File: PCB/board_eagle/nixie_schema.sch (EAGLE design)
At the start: 55 parts, among them IC1 LM2672M

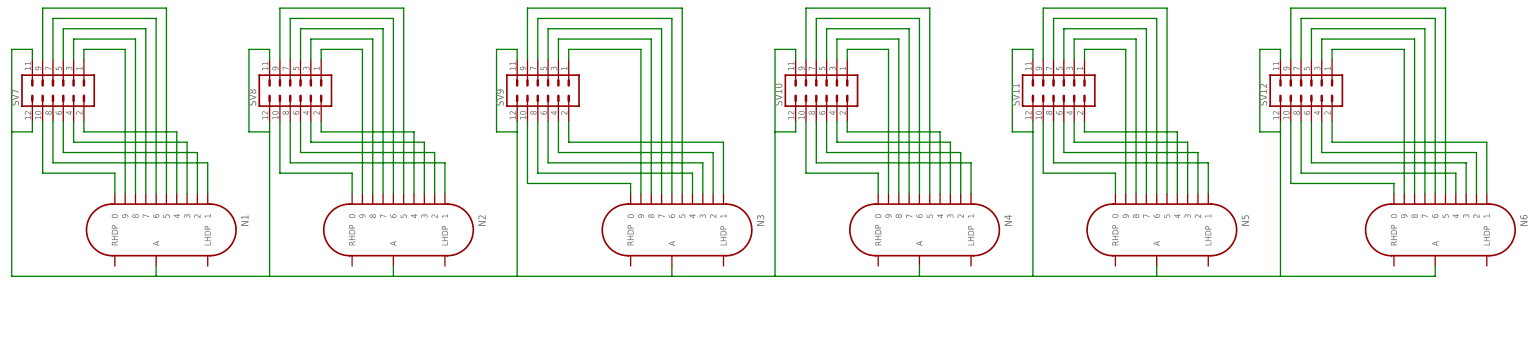
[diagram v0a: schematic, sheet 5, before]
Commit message: Fixing minor schematic issues (anode resistors and cap values in 3v3 PSU). Updated gitignore with EAGLE temp files
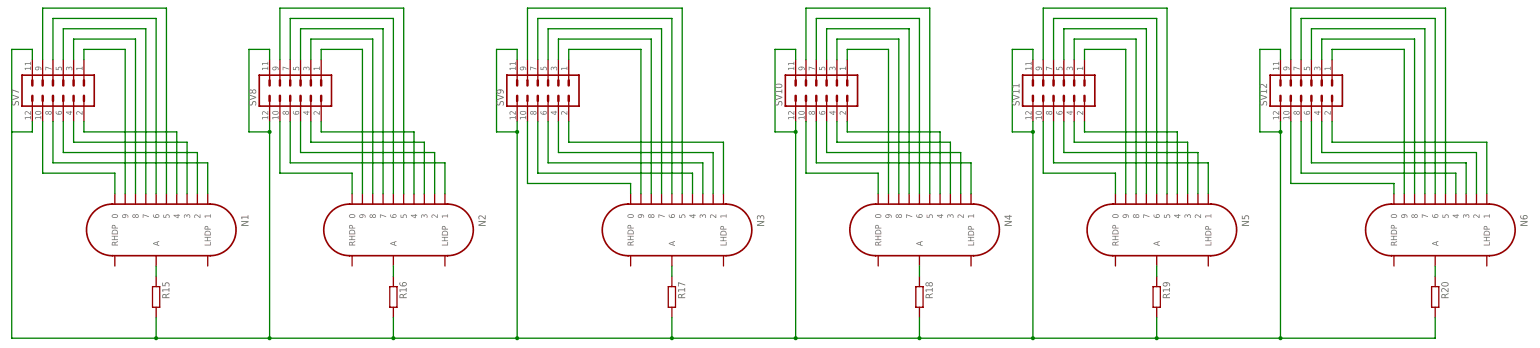
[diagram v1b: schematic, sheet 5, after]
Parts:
- added R15, R16, R17, R18, R19, R20: (no value), resistor:R-EU_R0603
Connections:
- removed net N$74: N1.A, N2.A, N3.A, N4.A, N5.A, N6.A, SV10.11, SV10.12, SV11.11, SV11.12, SV12.11, SV12.12, SV7.11, SV7.12, SV8.11, SV8.12, SV9.11, SV9.12
- new net N$45: R15.2, R16.2, R17.2, R18.2, R19.2, R20.2, SV10.11, SV10.12, SV11.11, SV11.12, SV12.11, SV12.12, SV7.11, SV7.12, SV8.11, SV8.12, SV9.11, SV9.12
- new net N$89: N6.A, R20.1
- new net N$90: N5.A, R19.1
- new net N$91: N4.A, R18.1
- new net N$92: N3.A, R17.1
- new net N$93: N2.A, R16.1
- new net N$94: N1.A, R15.1
- net GND: now also C6.C1; no longer C5.C1
- net N$11: now also C5.C1; no longer C6.C1
- net N$12: now also C5.C2; no longer C6.C2
- net N$5: now also C6.C2; no longer C5.C2
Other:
- moved on the sheet: C5, C6

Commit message: Most of HV supply schematic done. Need to pick transistors, caps and diode
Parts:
- added C10, C11: 680p, eagle-ltspice:C
- added D1: (no value), diode:DIODE-SOD123
- added Q1: (no value), semicon-smd-ipc:PNP-TRANSISTOR_SOT23
- added Q2: IRF3704S, transistor-power:IRF3704S
- added R21: 1k, resistor:R-EU_R0603
- added R22, R23: (no value), eagle-ltspice:RR1210
- added R24: 330k, resistor:R-EU_R0603
- added R25: 3.3k, resistor:R-EU_R0603
- added R26: 5.6k, resistor:R-EU_R0603
- added U$18: MC34063, MC34063:MC34063
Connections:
- new net N$74: C10.1, U$18.CT
- new net N$85: D1.A, Q1.B, R21.1, U$18.ES
- new net N$86: Q2.D
- new net N$87: R22.2, R23.2, U$18.CD, U$18.CS, U$18.IS
- new net N$95: D1.C, Q1.E, Q2.G
- new net N$96: C11.1, R24.2, R25.1, R26.1, U$18.CMP
- new net N$97: R26.2
- net GND: now also C10.2, C11.2, Q1.C, Q2.S, R21.2, R25.2, U$18.GND
- net HV_IN+: now also R24.1
- net VCC: now also R22.1, R23.1, U$18.VCC

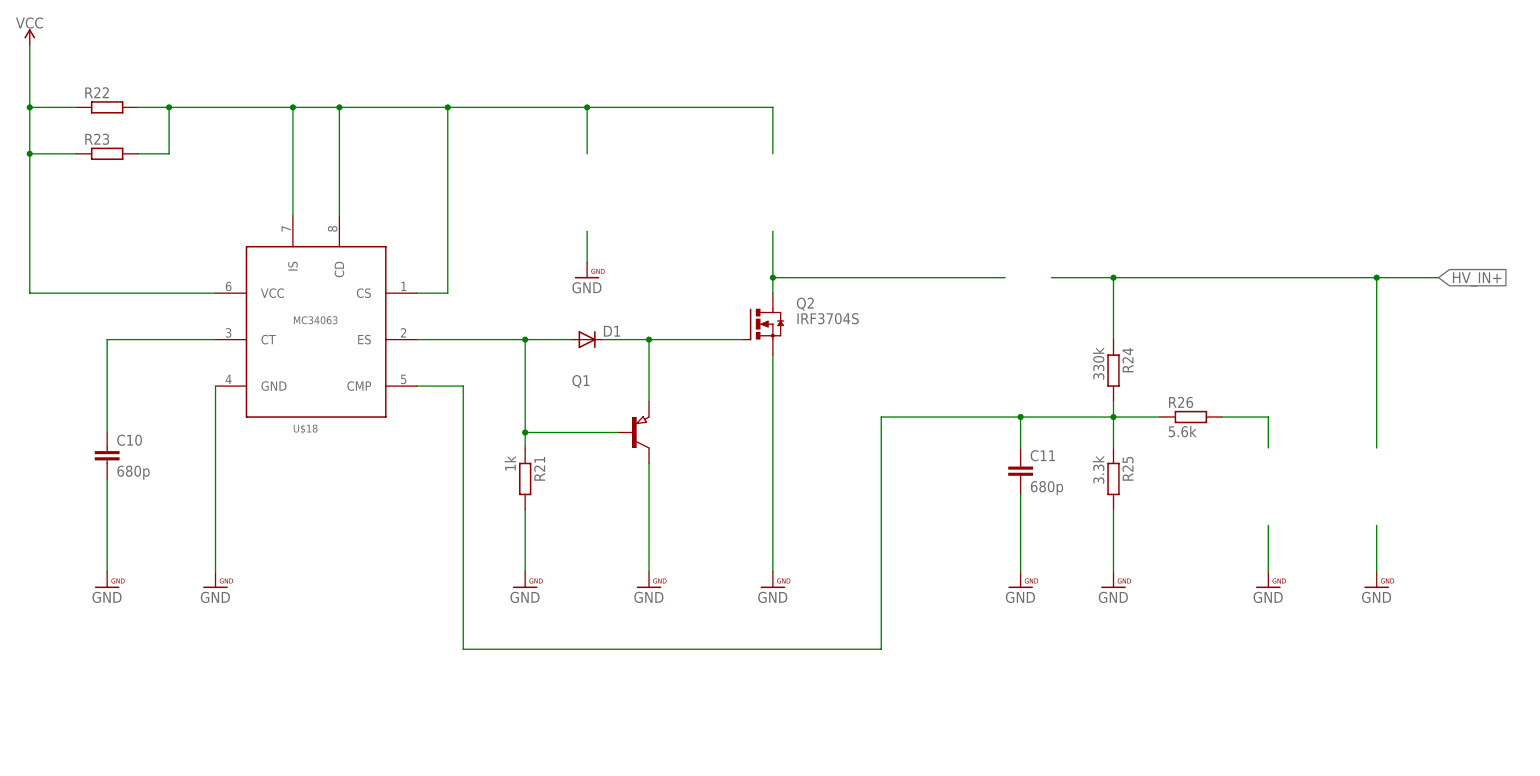
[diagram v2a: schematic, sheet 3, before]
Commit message: HV PSU schematic captured. Still need to pick correct pot
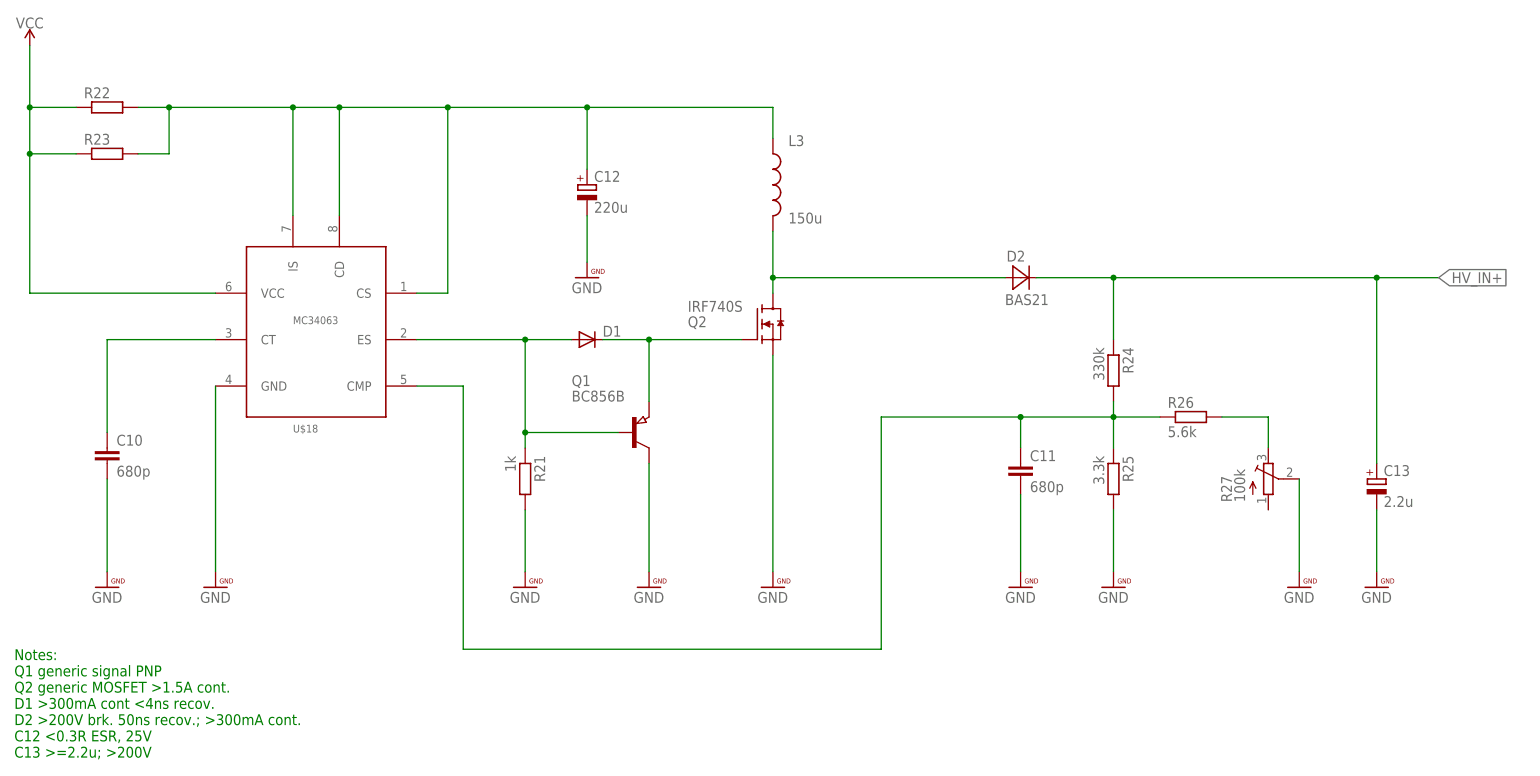
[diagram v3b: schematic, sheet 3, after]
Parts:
- added C12: 220u, rcl:CPOL-EU153CLV-0810
- added C13: 2.2u, rcl:CPOL-EU153CLV-1014
- added D2: BAS21, nixe_cmp:BAS21
- added L3: 150u, nixe_cmp:HM78D-128151KLFTR
- added R27: 100k, pot:TRIM_EU-SM-42/43X
- Q1: value (none) -> BC856B; device semicon-smd-ipc:PNP-TRANSISTOR_SOT23 -> nixe_cmp:BC856B
- Q2: value IRF3704S -> IRF740S; device transistor-power:IRF3704S -> nixe_cmp:IRF740S
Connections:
- net GND: now also C12.-, C13.-, R27.S
- net HV_IN+: now also C13.+, D2.C
- net N$86: now also D2.A, L3.2
- net N$87: now also C12.+, L3.1
- net N$97: now also R27.E
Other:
- note added: "Notes: Q1 generic signal PNP Q2 generic MOSFET >1.5A cont. D1 >300mA cont <4ns recov. D2 >200V brk. 50ns recov.; >300mA cont. C12 <0.3R ESR, 25V C13 >=2.2u; >200V"
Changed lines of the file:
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@@
 <part name="SUPPLY7" library="SparkFun-PowerSymbols" deviceset="VCC" device=""/>
 <part name="D1" library="diode" deviceset="DIODE-" device="SOD123"/>
-<part name="Q1" library="semicon-smd-ipc" deviceset="PNP-TRANSISTOR_" device="SOT23"/>
 <part name="U$22" library="PatternAgents-Beautify" deviceset="GND" device=""/>
-<part name="Q2" library="transistor-power" deviceset="IRF3704" device="S"/>
 <part name="U$23" library="PatternAgents-Beautify" deviceset="GND" device=""/>
 <part name="R24" library="resistor" deviceset="R-EU_" device="R0603" value="330k"/>
@@
 <part name="U$27" library="PatternAgents-Beautify" deviceset="GND" device=""/>
 <part name="U$28" library="PatternAgents-Beautify" deviceset="GND" device=""/>
+<part name="Q2" library="nixe_cmp" deviceset="IRF740S" device=""/>
+<part name="D2" library="nixe_cmp" deviceset="BAS21" device=""/>
+<part name="Q1" library="nixe_cmp" deviceset="BC856B" device=""/>
+<part name="L3" library="nixe_cmp" deviceset="HM78D-128151KLFTR" device="" value="150u"/>
+<part name="C12" library="rcl" deviceset="CPOL-EU" device="153CLV-0810" value="220u"/>
+<part name="C13" library="rcl" deviceset="CPOL-EU" device="153CLV-1014" value="2.2u"/>
+<part name="R27" library="pot" deviceset="TRIM_EU-" device="SM-42/43X" value="100k"/>
 </parts>
 <sheets>
@@
 <description>Power supply High Voltage</description>
 <plain>
+<text x="-5.08" y="-27.94" size="1.778" layer="91">Notes:
+Q1 generic signal PNP
+Q2 generic MOSFET &gt;1.5A cont.
+D1 &gt;300mA cont &lt;4ns recov.
+D2 &gt;200V brk. 50ns recov.; &gt;300mA cont.
+C12 &lt;0.3R ESR, 25V
+C13 &gt;=2.2u; &gt;200V</text>
 </plain>
 <instances>
@@
 <instance part="SUPPLY7" gate="G$1" x="-2.54" y="88.9"/>
 <instance part="D1" gate="G$1" x="88.9" y="40.64"/>
-<instance part="Q1" gate="G$1" x="96.52" y="25.4"/>
 <instance part="U$22" gate="G$1" x="99.06" y="2.54"/>
-<instance part="Q2" gate="G$1" x="116.84" y="43.18"/>
 <instance part="U$23" gate="G$1" x="119.38" y="2.54"/>
 <instance part="R24" gate="G$1" x="175.26" y="35.56" rot="R270"/>
@@
 <instance part="U$25" gate="G$1" x="160.02" y="2.54"/>
 <instance part="U$26" gate="G$1" x="88.9" y="53.34"/>
-<instance part="U$27" gate="G$1" x="200.66" y="2.54"/>
+<instance part="U$27" gate="G$1" x="205.74" y="2.54"/>
 <instance part="U$28" gate="G$1" x="218.44" y="2.54"/>
+<instance part="Q2" gate="G$1" x="116.84" y="43.18"/>
+<instance part="D2" gate="D$1" x="160.02" y="50.8"/>
+<instance part="Q1" gate="Q$1" x="96.52" y="25.4"/>
+<instance part="L3" gate="G$1" x="119.38" y="66.04"/>
+<instance part="C12" gate="G$1" x="88.9" y="66.04"/>
+<instance part="C13" gate="G$1" x="218.44" y="17.78"/>
+<instance part="R27" gate="1" x="200.66" y="17.78"/>
 </instances>
 <busses>
@@
 <segment>
 <pinref part="U$22" gate="G$1" pin="GND"/>
-<pinref part="Q1" gate="G$1" pin="C"/>
 <wire x1="99.06" y1="2.54" x2="99.06" y2="20.32" width="0.1524" layer="91"/>
+<pinref part="Q1" gate="Q$1" pin="C"/>
 </segment>
 <segment>
 <pinref part="U$23" gate="G$1" pin="GND"/>
+<wire x1="119.38" y1="2.54" x2="119.38" y2="38.1" width="0.1524" layer="91"/>
 <pinref part="Q2" gate="G$1" pin="S"/>
-<wire x1="119.38" y1="2.54" x2="119.38" y2="38.1" width="0.1524" layer="91"/>
 </segment>
 <segment>
@@
 <segment>
 <pinref part="U$26" gate="G$1" pin="GND"/>
-<wire x1="88.9" y1="53.34" x2="88.9" y2="58.42" width="0.1524" layer="91"/>
+<wire x1="88.9" y1="53.34" x2="88.9" y2="60.96" width="0.1524" layer="91"/>
+<pinref part="C12" gate="G$1" pin="-"/>
 </segment>
 <segment>
 <pinref part="U$27" gate="G$1" pin="GND"/>
-<wire x1="200.66" y1="2.54" x2="200.66" y2="10.16" width="0.1524" layer="91"/>
+<pinref part="R27" gate="1" pin="S"/>
+<wire x1="205.74" y1="2.54" x2="205.74" y2="17.78" width="0.1524" layer="91"/>
 </segment>
 <segment>
 <pinref part="U$28" gate="G$1" pin="GND"/>
-<wire x1="218.44" y1="2.54" x2="218.44" y2="10.16" width="0.1524" layer="91"/>
+<wire x1="218.44" y1="2.54" x2="218.44" y2="12.7" width="0.1524" layer="91"/>
+<pinref part="C13" gate="G$1" pin="-"/>
 </segment>
 </net>
@@
 <wire x1="86.36" y1="40.64" x2="78.74" y2="40.64" width="0.1524" layer="91"/>
 <junction x="78.74" y="40.64"/>
-<pinref part="Q1" gate="G$1" pin="B"/>
 <wire x1="93.98" y1="25.4" x2="78.74" y2="25.4" width="0.1524" layer="91"/>
 <junction x="78.74" y="25.4"/>
+<pinref part="Q1" gate="Q$1" pin="B"/>
 </segment>
 </net>
@@
 <wire x1="66.04" y1="78.74" x2="88.9" y2="78.74" width="0.1524" layer="91"/>
 <wire x1="88.9" y1="78.74" x2="119.38" y2="78.74" width="0.1524" layer="91"/>
-<wire x1="119.38" y1="78.74" x2="119.38" y2="71.12" width="0.1524" layer="91"/>
 <junction x="66.04" y="78.74"/>
-<wire x1="88.9" y1="78.74" x2="88.9" y2="71.12" width="0.1524" layer="91"/>
+<wire x1="88.9" y1="78.74" x2="88.9" y2="68.58" width="0.1524" layer="91"/>
 <junction x="88.9" y="78.74"/>
+<wire x1="119.38" y1="78.74" x2="119.38" y2="73.66" width="0.1524" layer="91"/>
+<pinref part="L3" gate="G$1" pin="1"/>
+<pinref part="C12" gate="G$1" pin="+"/>
 </segment>
 </net>
@@
 <net name="N$95" class="0">
 <segment>
-<pinref part="Q1" gate="G$1" pin="E"/>
 <wire x1="99.06" y1="30.48" x2="99.06" y2="40.64" width="0.1524" layer="91"/>
 <pinref part="D1" gate="G$1" pin="C"/>
 <wire x1="99.06" y1="40.64" x2="91.44" y2="40.64" width="0.1524" layer="91"/>
-<pinref part="Q2" gate="G$1" pin="G"/>
 <wire x1="114.3" y1="40.64" x2="99.06" y2="40.64" width="0.1524" layer="91"/>
 <junction x="99.06" y="40.64"/>
+<pinref part="Q2" gate="G$1" pin="G"/>
+<pinref part="Q1" gate="Q$1" pin="E"/>
 </segment>
 </net>
@@
 <label x="228.6" y="50.8" size="1.778" layer="95" xref="yes"/>
 <wire x1="218.44" y1="50.8" x2="228.6" y2="50.8" width="0.1524" layer="91"/>
-<wire x1="175.26" y1="50.8" x2="165.1" y2="50.8" width="0.1524" layer="91"/>
+<wire x1="175.26" y1="50.8" x2="162.56" y2="50.8" width="0.1524" layer="91"/>
 <junction x="175.26" y="50.8"/>
-<wire x1="218.44" y1="50.8" x2="218.44" y2="22.86" width="0.1524" layer="91"/>
+<wire x1="218.44" y1="50.8" x2="218.44" y2="20.32" width="0.1524" layer="91"/>
 <junction x="218.44" y="50.8"/>
+<pinref part="D2" gate="D$1" pin="C"/>
+<pinref part="C13" gate="G$1" pin="+"/>
 </segment>
 </net>
 <net name="N$86" class="0">
 <segment>
-<pinref part="Q2" gate="G$1" pin="D"/>
 <wire x1="119.38" y1="48.26" x2="119.38" y2="50.8" width="0.1524" layer="91"/>
 <wire x1="119.38" y1="50.8" x2="119.38" y2="58.42" width="0.1524" layer="91"/>
 <wire x1="157.48" y1="50.8" x2="119.38" y2="50.8" width="0.1524" layer="91"/>
 <junction x="119.38" y="50.8"/>
+<pinref part="Q2" gate="G$1" pin="D"/>
+<pinref part="D2" gate="D$1" pin="A"/>
+<pinref part="L3" gate="G$1" pin="2"/>
 </segment>
 </net>
@@
 <wire x1="193.04" y1="27.94" x2="200.66" y2="27.94" width="0.1524" layer="91"/>
 <wire x1="200.66" y1="27.94" x2="200.66" y2="22.86" width="0.1524" layer="91"/>
+<pinref part="R27" gate="1" pin="E"/>
 </segment>
 </net>
@@
 </schematic>
 </drawing>
+<compatibility>
+<note version="6.3" minversion="6.2.2" severity="warning">
+Since Version 6.2.2 text objects can contain more than one line,
+which will not be processed correctly with this version.
+</note>
+</compatibility>
 </eagle>
